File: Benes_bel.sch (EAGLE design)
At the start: 19 parts, among them J1 DCJ0202, K1 HE751, K2 HE751, K3 HE751, K4 HE751, T1 BC337, T2 BC337, T3 BC337, T4 BC337, X5 FH12-08S-1SH

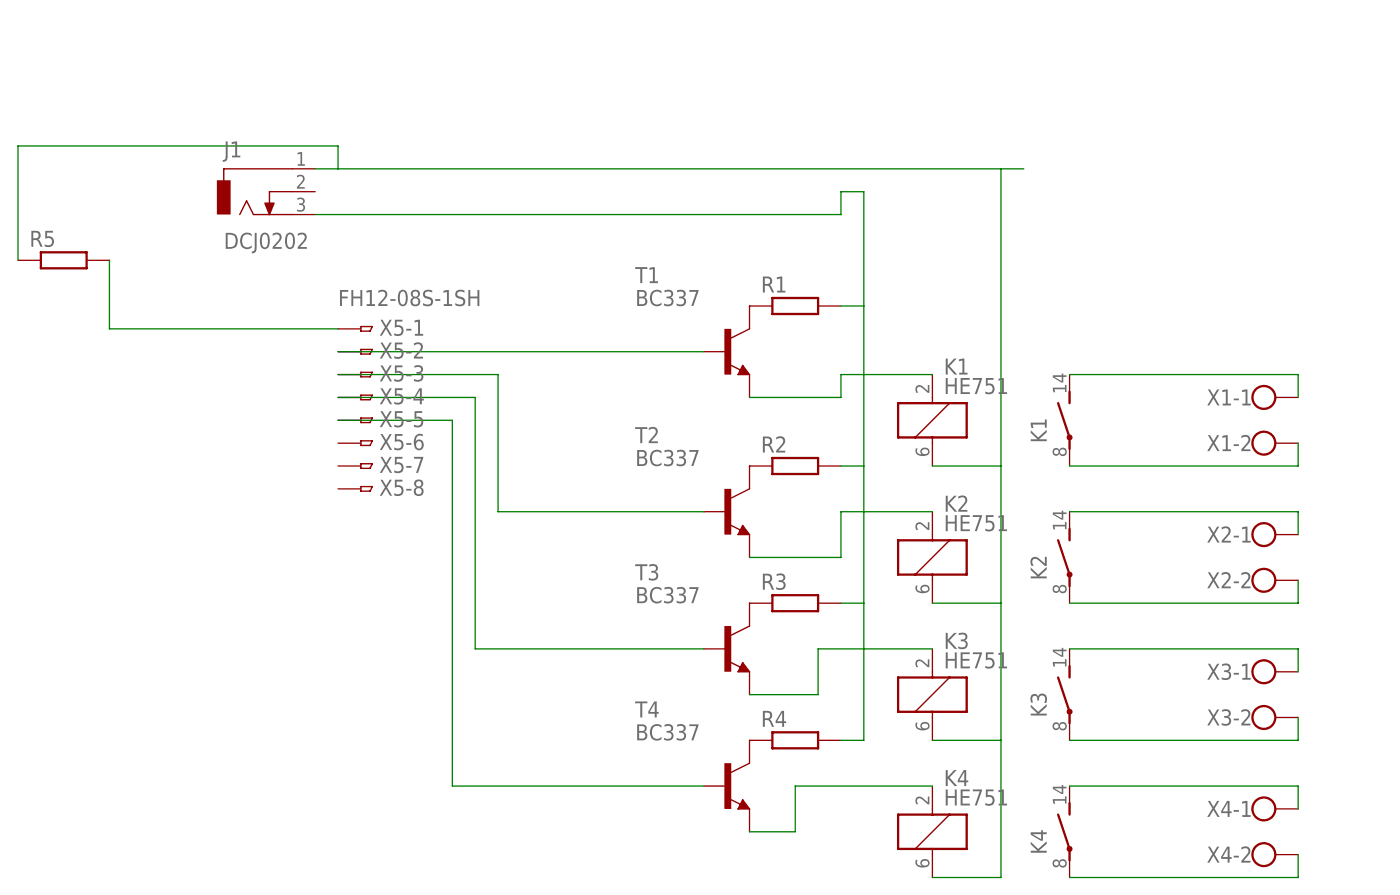
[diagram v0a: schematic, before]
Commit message: aanpassing met extra leds als controle tracks op 2 lagen Gerber files
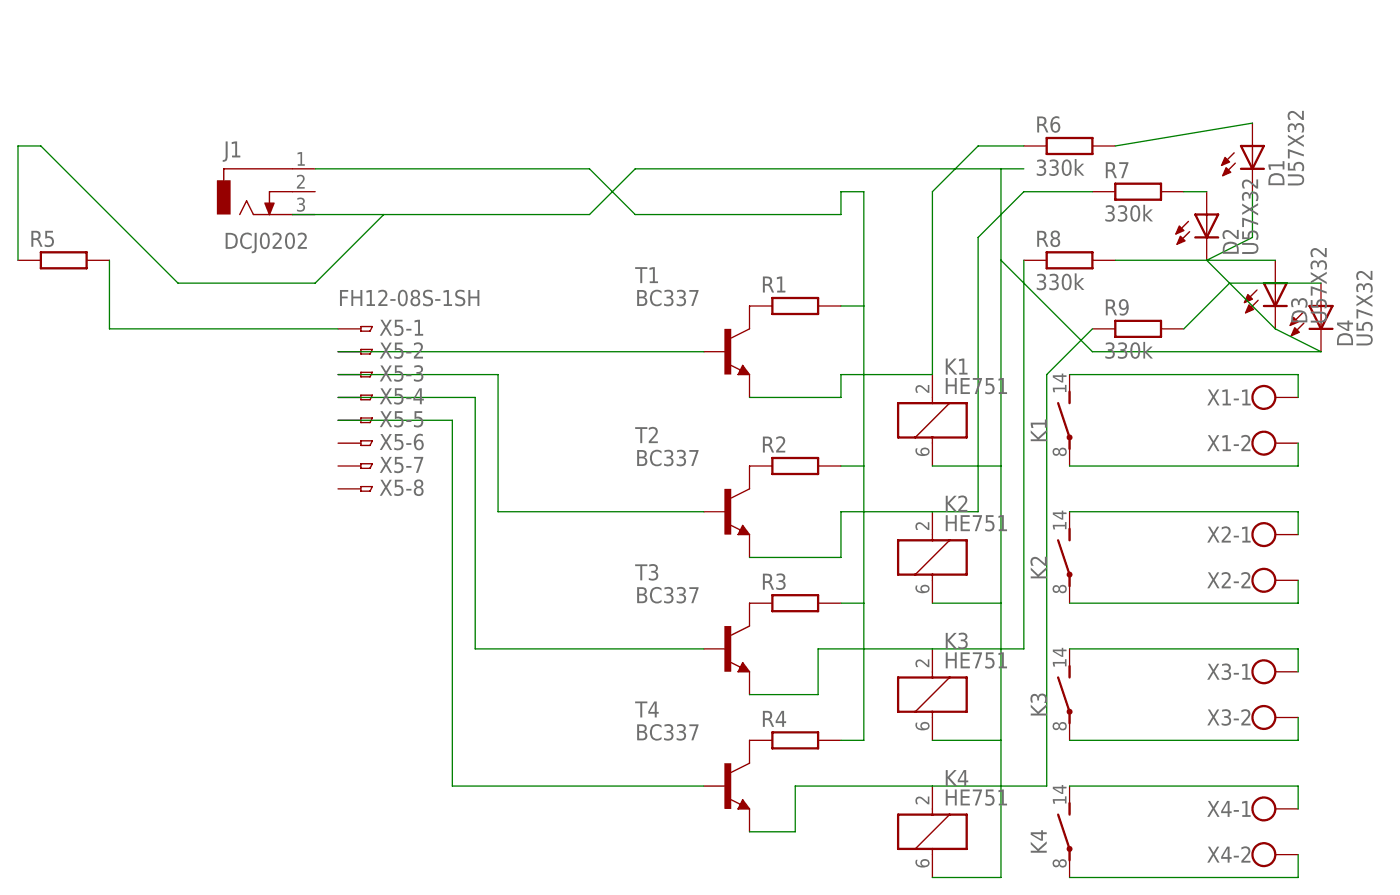
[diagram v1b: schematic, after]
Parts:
- added D1, D2, D3, D4: U57X32, led:U57X32
- added R6, R7, R8, R9: 330k, resistor:R-EU_0207/12
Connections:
- removed net N$21: J1.1, K11.2, K21.2, K31.2, K41.2, R5.1
- new net N$24: D4.A, R9.2
- new net N$25: D1.A, R6.2
- new net N$26: D2.A, R7.2
- new net N$27: D3.A, R8.2
- new net N$28: D1.C, D2.C, D3.C, D4.C, K11.2, K21.2, K31.2, K41.2, R5.1
- new net N$30: R8.1
- net N$20: now also R9.1
- net N$23: now also R6.1
- net N$5: now also R7.1
- net N$6: now also J1.1; no longer J1.3
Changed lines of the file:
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@@
 <part name="J1" library="con-jack" deviceset="DCJ0202" device=""/>
 <part name="R5" library="resistor" deviceset="R-EU_" device="0207/12"/>
+<part name="R6" library="resistor" deviceset="R-EU_" device="0207/12" value="330k"/>
+<part name="R7" library="resistor" deviceset="R-EU_" device="0207/12" value="330k"/>
+<part name="R8" library="resistor" deviceset="R-EU_" device="0207/12" value="330k"/>
+<part name="R9" library="resistor" deviceset="R-EU_" device="0207/12" value="330k"/>
+<part name="D1" library="led" deviceset="U57X32" device=""/>
+<part name="D2" library="led" deviceset="U57X32" device=""/>
+<part name="D3" library="led" deviceset="U57X32" device=""/>
+<part name="D4" library="led" deviceset="U57X32" device=""/>
 </parts>
 <sheets>
@@
 <instance part="J1" gate="G$1" x="-2.54" y="111.76"/>
 <instance part="R5" gate="G$1" x="-22.86" y="104.14"/>
+<instance part="R6" gate="G$1" x="88.9" y="116.84"/>
+<instance part="R7" gate="G$1" x="96.52" y="111.76"/>
+<instance part="R8" gate="G$1" x="88.9" y="104.14"/>
+<instance part="R9" gate="G$1" x="96.52" y="96.52"/>
+<instance part="D1" gate="1" x="109.22" y="116.84"/>
+<instance part="D2" gate="1" x="104.14" y="109.22"/>
+<instance part="D3" gate="1" x="111.76" y="101.6"/>
+<instance part="D4" gate="1" x="116.84" y="99.06"/>
 </instances>
 <busses>
@@
 <pinref part="R4" gate="G$1" pin="2"/>
 <wire x1="66.04" y1="50.8" x2="63.5" y2="50.8" width="0.1524" layer="91"/>
-<pinref part="J1" gate="G$1" pin="3"/>
-<wire x1="5.08" y1="109.22" x2="63.5" y2="109.22" width="0.1524" layer="91"/>
 <wire x1="63.5" y1="109.22" x2="63.5" y2="111.76" width="0.1524" layer="91"/>
 <wire x1="63.5" y1="111.76" x2="66.04" y2="111.76" width="0.1524" layer="91"/>
+<wire x1="63.5" y1="109.22" x2="40.64" y2="109.22" width="0.1524" layer="91"/>
+<wire x1="40.64" y1="109.22" x2="35.56" y2="114.3" width="0.1524" layer="91"/>
+<pinref part="J1" gate="G$1" pin="1"/>
+<wire x1="35.56" y1="114.3" x2="5.08" y2="114.3" width="0.1524" layer="91"/>
 </segment>
 </net>
@@
 <wire x1="63.5" y1="91.44" x2="63.5" y2="88.9" width="0.1524" layer="91"/>
 <wire x1="63.5" y1="88.9" x2="53.34" y2="88.9" width="0.1524" layer="91"/>
+<pinref part="R6" gate="G$1" pin="1"/>
+<wire x1="83.82" y1="116.84" x2="78.74" y2="116.84" width="0.1524" layer="91"/>
+<wire x1="78.74" y1="116.84" x2="73.66" y2="111.76" width="0.1524" layer="91"/>
+<wire x1="73.66" y1="111.76" x2="73.66" y2="91.44" width="0.1524" layer="91"/>
 </segment>
 </net>
@@
 <wire x1="63.5" y1="76.2" x2="63.5" y2="71.12" width="0.1524" layer="91"/>
 <wire x1="63.5" y1="71.12" x2="53.34" y2="71.12" width="0.1524" layer="91"/>
+<pinref part="R7" gate="G$1" pin="1"/>
+<wire x1="91.44" y1="111.76" x2="83.82" y2="111.76" width="0.1524" layer="91"/>
+<wire x1="83.82" y1="111.76" x2="78.74" y2="106.68" width="0.1524" layer="91"/>
+<wire x1="78.74" y1="106.68" x2="78.74" y2="76.2" width="0.1524" layer="91"/>
+<wire x1="78.74" y1="76.2" x2="73.66" y2="76.2" width="0.1524" layer="91"/>
 </segment>
 </net>
@@
 <wire x1="58.42" y1="45.72" x2="58.42" y2="40.64" width="0.1524" layer="91"/>
 <wire x1="58.42" y1="40.64" x2="53.34" y2="40.64" width="0.1524" layer="91"/>
-</segment>
-</net>
-<net name="N$21" class="0">
-<segment>
+<pinref part="R9" gate="G$1" pin="1"/>
+<wire x1="91.44" y1="96.52" x2="86.36" y2="91.44" width="0.1524" layer="91"/>
+<wire x1="86.36" y1="91.44" x2="86.36" y2="45.72" width="0.1524" layer="91"/>
+<wire x1="86.36" y1="45.72" x2="73.66" y2="45.72" width="0.1524" layer="91"/>
+</segment>
+</net>
+<net name="N$22" class="0">
+<segment>
+<pinref part="X5" gate="-1" pin="1"/>
+<wire x1="7.62" y1="96.52" x2="-17.78" y2="96.52" width="0.1524" layer="91"/>
+<pinref part="R5" gate="G$1" pin="2"/>
+<wire x1="-17.78" y1="96.52" x2="-17.78" y2="104.14" width="0.1524" layer="91"/>
+</segment>
+</net>
+<net name="N$25" class="0">
+<segment>
+<pinref part="D1" gate="1" pin="A"/>
+<pinref part="R6" gate="G$1" pin="2"/>
+<wire x1="109.22" y1="119.38" x2="93.98" y2="116.84" width="0.1524" layer="91"/>
+</segment>
+</net>
+<net name="N$26" class="0">
+<segment>
+<pinref part="D2" gate="1" pin="A"/>
+<pinref part="R7" gate="G$1" pin="2"/>
+<wire x1="104.14" y1="111.76" x2="101.6" y2="111.76" width="0.1524" layer="91"/>
+</segment>
+</net>
+<net name="N$27" class="0">
+<segment>
+<pinref part="R8" gate="G$1" pin="2"/>
+<pinref part="D3" gate="1" pin="A"/>
+<wire x1="93.98" y1="104.14" x2="111.76" y2="104.14" width="0.1524" layer="91"/>
+</segment>
+</net>
+<net name="N$24" class="0">
+<segment>
+<pinref part="D4" gate="1" pin="A"/>
+<pinref part="R9" gate="G$1" pin="2"/>
+<wire x1="116.84" y1="101.6" x2="106.68" y2="101.6" width="0.1524" layer="91"/>
+<wire x1="106.68" y1="101.6" x2="101.6" y2="96.52" width="0.1524" layer="91"/>
+</segment>
+</net>
+<net name="N$30" class="0">
+<segment>
+<pinref part="R8" gate="G$1" pin="1"/>
+<wire x1="83.82" y1="104.14" x2="83.82" y2="60.96" width="0.1524" layer="91"/>
+<wire x1="83.82" y1="60.96" x2="73.66" y2="60.96" width="0.1524" layer="91"/>
+</segment>
+</net>
+<net name="N$28" class="0">
+<segment>
+<pinref part="R5" gate="G$1" pin="1"/>
+<wire x1="-27.94" y1="104.14" x2="-27.94" y2="116.84" width="0.1524" layer="91"/>
+<wire x1="-27.94" y1="116.84" x2="-25.4" y2="116.84" width="0.1524" layer="91"/>
+<wire x1="-25.4" y1="116.84" x2="-10.16" y2="101.6" width="0.1524" layer="91"/>
+<wire x1="-10.16" y1="101.6" x2="5.08" y2="101.6" width="0.1524" layer="91"/>
 <pinref part="K4" gate="1" pin="2"/>
 <wire x1="73.66" y1="35.56" x2="81.28" y2="35.56" width="0.1524" layer="91"/>
@@
 <pinref part="K1" gate="1" pin="2"/>
 <wire x1="81.28" y1="81.28" x2="73.66" y2="81.28" width="0.1524" layer="91"/>
-<pinref part="J1" gate="G$1" pin="1"/>
-<wire x1="5.08" y1="114.3" x2="7.62" y2="114.3" width="0.1524" layer="91"/>
-<wire x1="7.62" y1="114.3" x2="81.28" y2="114.3" width="0.1524" layer="91"/>
 <wire x1="83.82" y1="114.3" x2="81.28" y2="114.3" width="0.1524" layer="91"/>
-<wire x1="81.28" y1="114.3" x2="81.28" y2="81.28" width="0.1524" layer="91"/>
-<wire x1="-27.94" y1="116.84" x2="7.62" y2="116.84" width="0.1524" layer="91"/>
-<wire x1="7.62" y1="116.84" x2="7.62" y2="114.3" width="0.1524" layer="91"/>
-<pinref part="R5" gate="G$1" pin="1"/>
-<wire x1="-27.94" y1="104.14" x2="-27.94" y2="116.84" width="0.1524" layer="91"/>
-</segment>
-</net>
-<net name="N$22" class="0">
-<segment>
-<pinref part="X5" gate="-1" pin="1"/>
-<wire x1="7.62" y1="96.52" x2="-17.78" y2="96.52" width="0.1524" layer="91"/>
-<pinref part="R5" gate="G$1" pin="2"/>
-<wire x1="-17.78" y1="96.52" x2="-17.78" y2="104.14" width="0.1524" layer="91"/>
-</segment>
-</net>
+<wire x1="81.28" y1="114.3" x2="81.28" y2="104.14" width="0.1524" layer="91"/>
+<wire x1="81.28" y1="104.14" x2="81.28" y2="81.28" width="0.1524" layer="91"/>
+<pinref part="D1" gate="1" pin="C"/>
+<pinref part="D2" gate="1" pin="C"/>
+<wire x1="109.22" y1="111.76" x2="109.22" y2="106.68" width="0.1524" layer="91"/>
+<wire x1="109.22" y1="106.68" x2="104.14" y2="104.14" width="0.1524" layer="91"/>
+<pinref part="D3" gate="1" pin="C"/>
+<wire x1="104.14" y1="104.14" x2="111.76" y2="96.52" width="0.1524" layer="91"/>
+<pinref part="D4" gate="1" pin="C"/>
+<wire x1="111.76" y1="96.52" x2="116.84" y2="93.98" width="0.1524" layer="91"/>
+<wire x1="116.84" y1="93.98" x2="91.44" y2="93.98" width="0.1524" layer="91"/>
+<wire x1="91.44" y1="93.98" x2="81.28" y2="104.14" width="0.1524" layer="91"/>
+<wire x1="81.28" y1="114.3" x2="40.64" y2="114.3" width="0.1524" layer="91"/>
+<wire x1="40.64" y1="114.3" x2="35.56" y2="109.22" width="0.1524" layer="91"/>
+<wire x1="35.56" y1="109.22" x2="12.7" y2="109.22" width="0.1524" layer="91"/>
+<wire x1="12.7" y1="109.22" x2="2.54" y2="109.22" width="0.1524" layer="91"/>
+<wire x1="5.08" y1="101.6" x2="12.7" y2="109.22" width="0.1524" layer="91"/>
+</segment>
+</net>
